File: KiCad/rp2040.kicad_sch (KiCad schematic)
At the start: 32 parts, among them SW1 SW_Push, U1 RP2040, U3 W25Q16JVSSIQ, Y1 12.000MHz

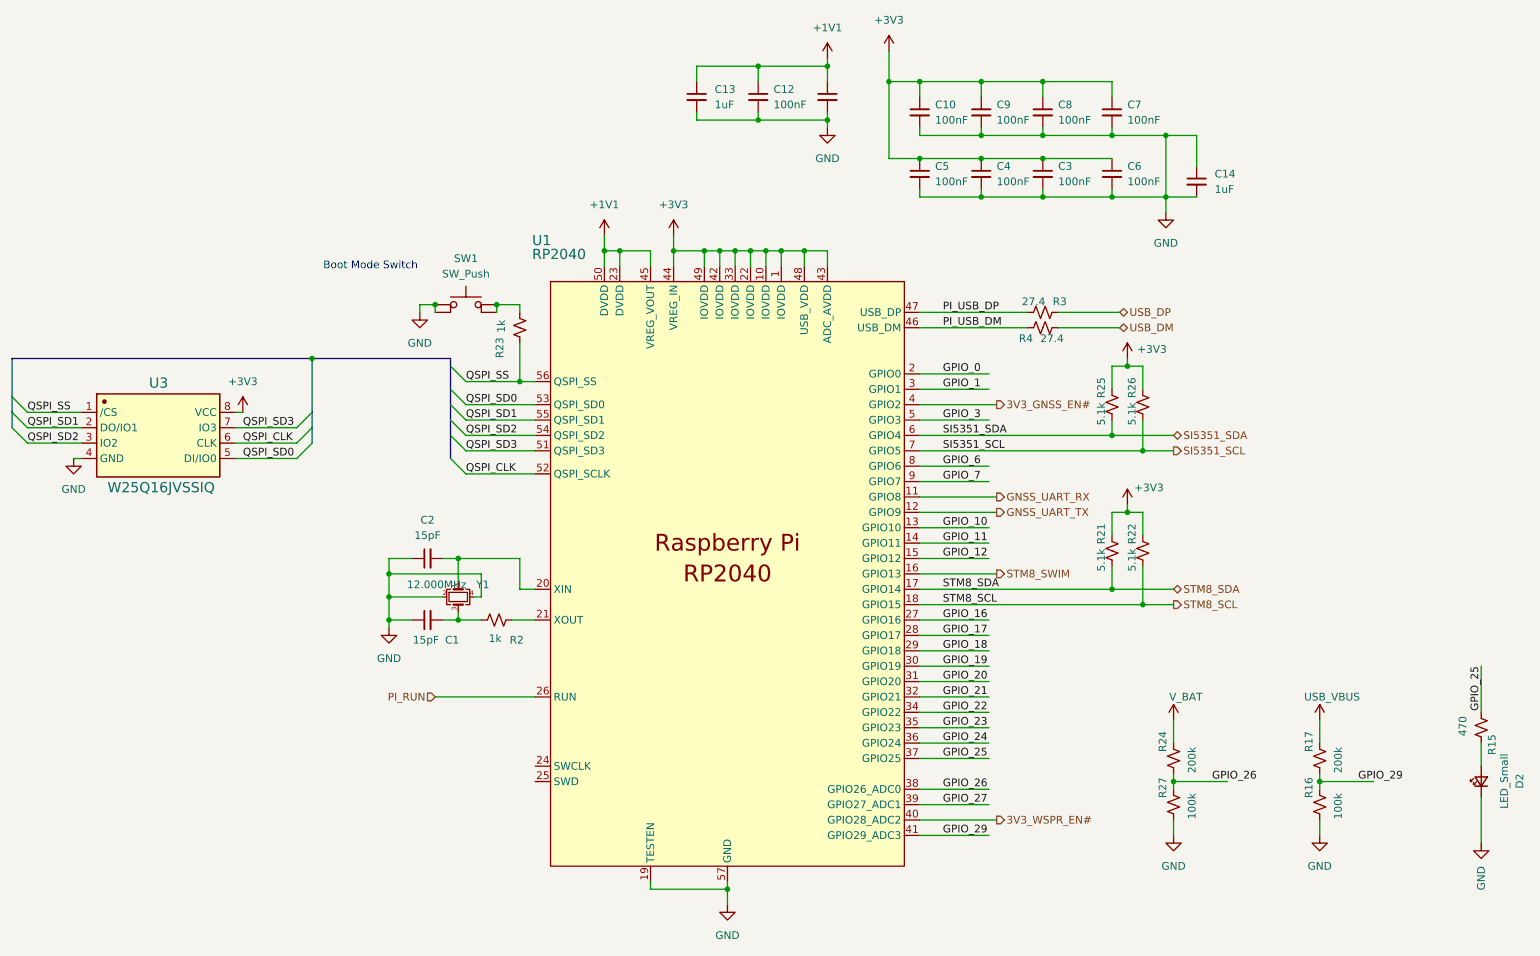
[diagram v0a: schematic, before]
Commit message: Start of docs and design incremental progress
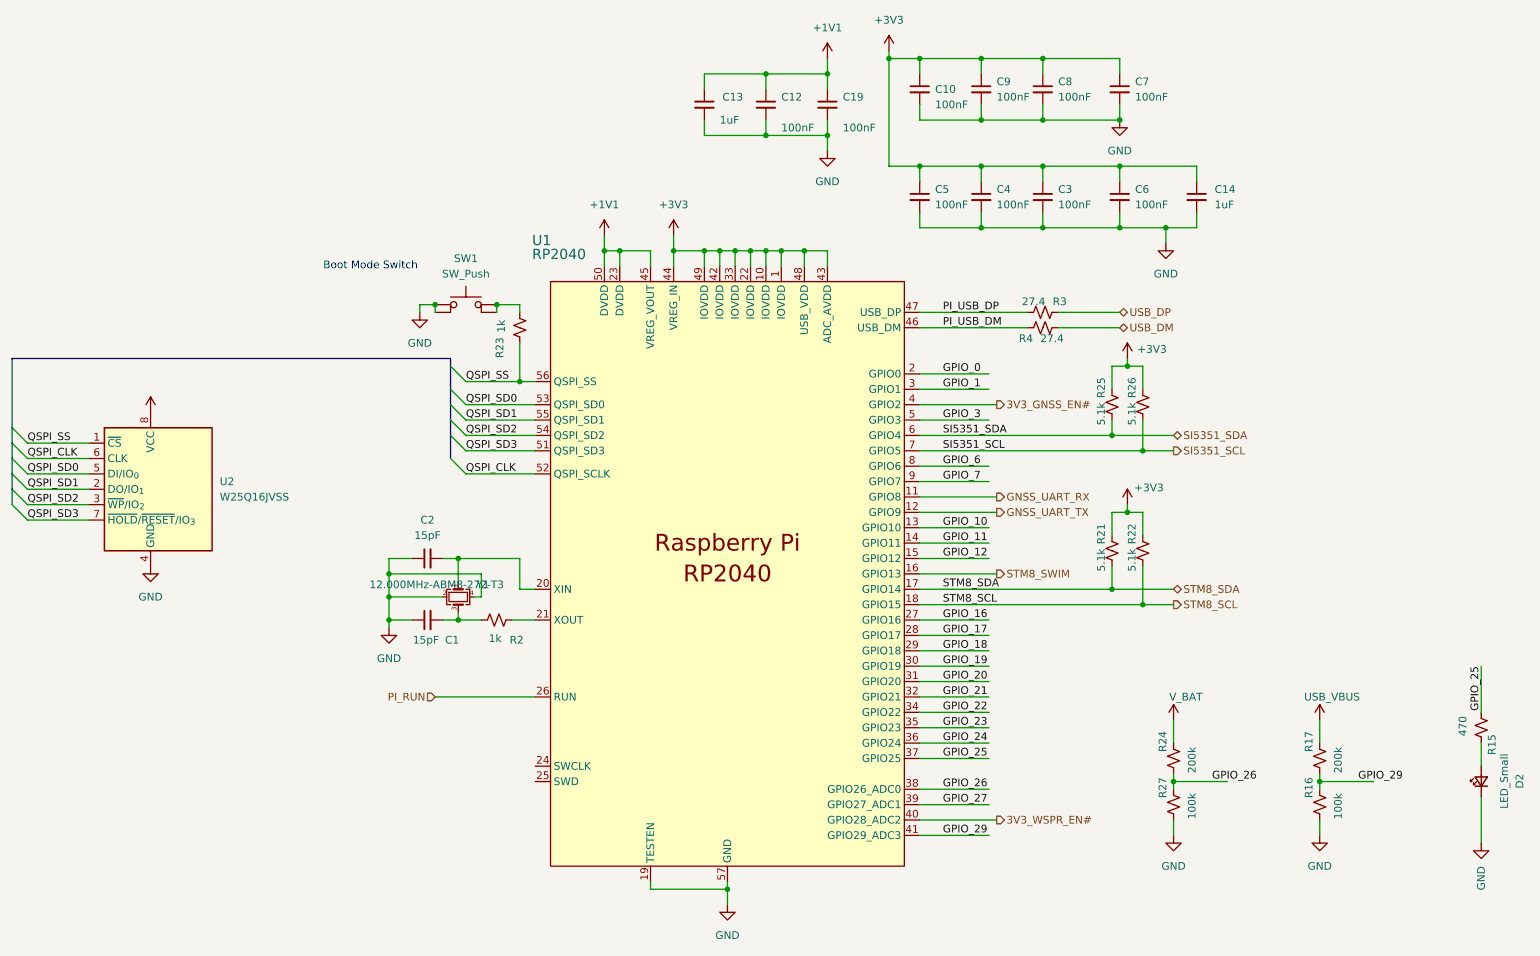
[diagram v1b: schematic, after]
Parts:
- removed C11: 100nF, Capacitor_SMD:C_0402_1005Metric, symbol Device:C_Small
- removed U3: W25Q16JVSSIQ, Package_SON:Winbond_USON-8-1EP_3x2mm_P0.5mm_EP0.2x1.6mm, symbol W25Q16JVSSIQ
- added C19: 100nF, Capacitor_SMD:C_0402_1005Metric, symbol Device:C_Small
- added U2: W25Q16JVSS, Package_SO:SOIC-8_5.3x5.3mm_P1.27mm, symbol Memory_Flash:W25Q16JVSS
- D2: footprint (none) -> LED_SMD:LED_0402_1005Metric
- U1: footprint JetBoard:LQFN-56_L7.0-W7.0-P0.4-EP -> Package_DFN_QFN:QFN-56-1EP_7x7mm_P0.4mm_EP3.2x3.2mm
- Y1: value 12.000MHz -> 12.000MHz-ABM8-272-T3; footprint (none) -> Crystal:Crystal_SMD_3225-4Pin_3.2x2.5mm
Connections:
- net +1V1: now also C19.1
- net +3V3: now also C14.1, U2.8 (VCC)
- net GND: now also SW1.2, C19.2, U2.4 (GND); no longer C14.1, SW1. (2)
- net QSPI_CLK: now also U2.6 (CLK)
- net QSPI_SD0: now also U2.5 (DI/IO_{0})
- net QSPI_SD1: now also U2.2 (DO/IO_{1})
- net QSPI_SD2: now also U2.3 (~{WP}/IO_{2})
- net QSPI_SD3: now also U2.7 (~{HOLD}/~{RESET}/IO_{3})
- net QSPI_SS: now also U2.1 (~{CS})
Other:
- moved on the sheet: C10, C12, C13, C14, C3, C4, C5, C6, C7, C8, C9

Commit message: Update schematic and board
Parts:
- U2: value W25Q16JVSS -> W25Q16JVUXIQ; footprint Package_SO:SOIC-8_5.3x5.3mm_P1.27mm -> Package_SON:Winbond_USON-8-1EP_3x2mm_P0.5mm_EP0.2x1.6mm
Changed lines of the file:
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@@
 			)
 		)
-		(property "Value" "W25Q16JVSS"
+		(property "Value" "W25Q16JVUXIQ"
 			(at 67.31 95.2499 0)
 			(effects
@@
 			)
 		)
-		(property "Footprint" "Package_SO:SOIC-8_5.3x5.3mm_P1.27mm"
+		(property "Footprint" "Package_SON:Winbond_USON-8-1EP_3x2mm_P0.5mm_EP0.2x1.6mm"
 			(at 55.88 93.98 0)
 			(effects
@@
 			)
 		)
-		(property "Description" "16Mbit / 2MiB Serial Flash Memory, Standard/Dual/Quad SPI, 2.7-3.6V, SOIC-8 (208 mil)"
+		(property "Description" "16Mbit / 2MiB Serial Flash Memory, Standard/Dual/Quad SPI, 2.7-3.6V"
 			(at 55.88 93.98 0)
 			(effects

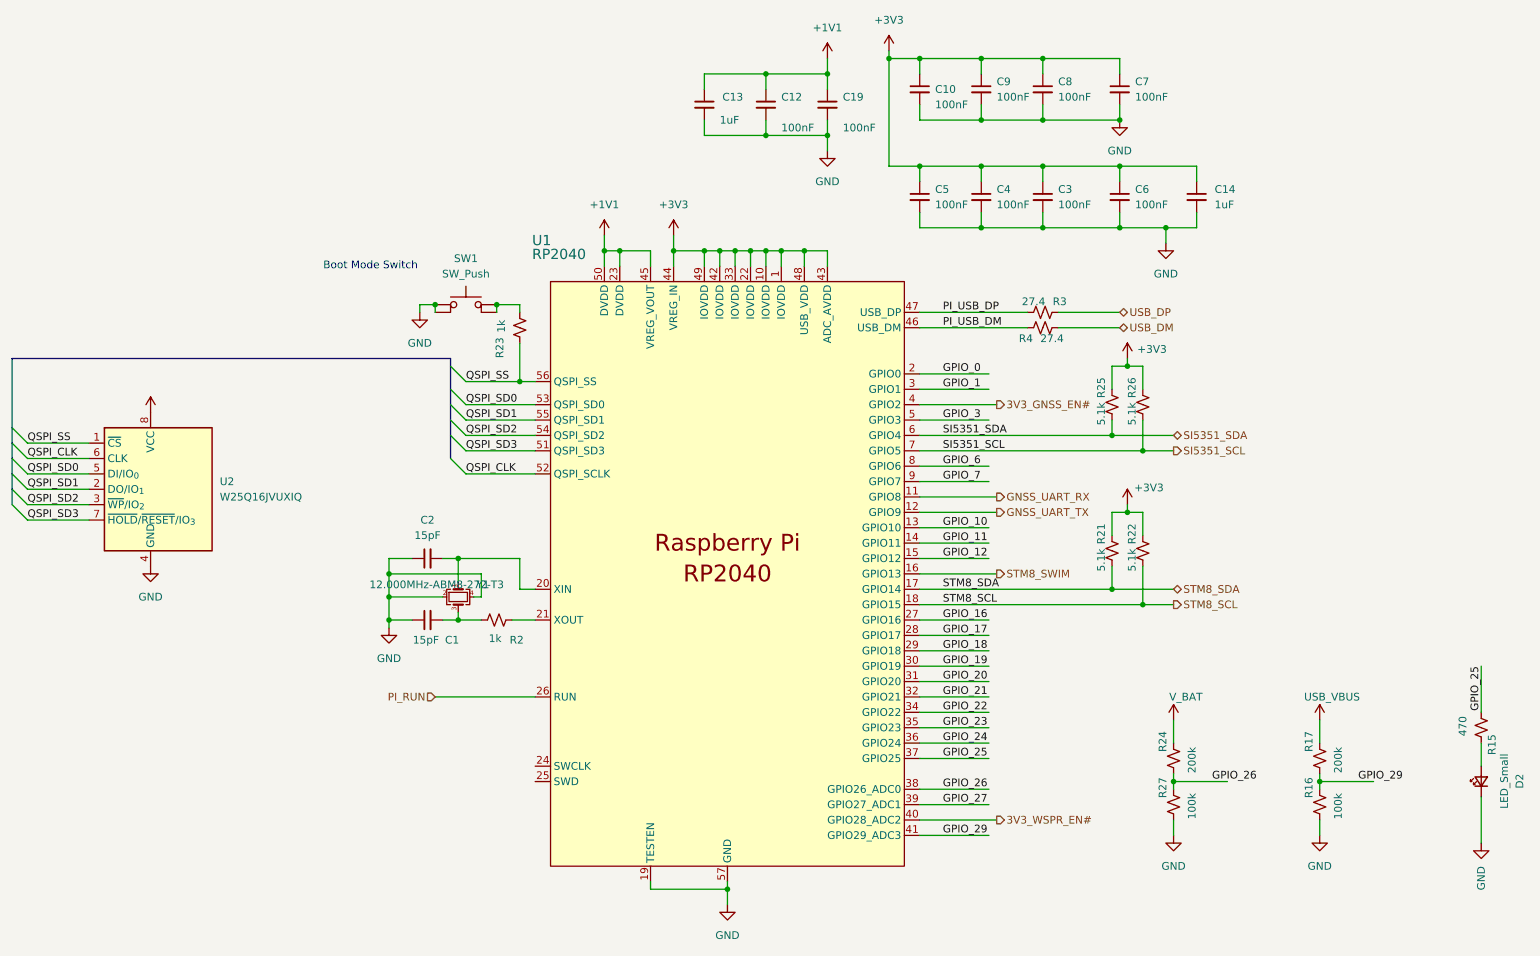
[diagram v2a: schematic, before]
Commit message: 3D model fixes and change to 3.0V buck
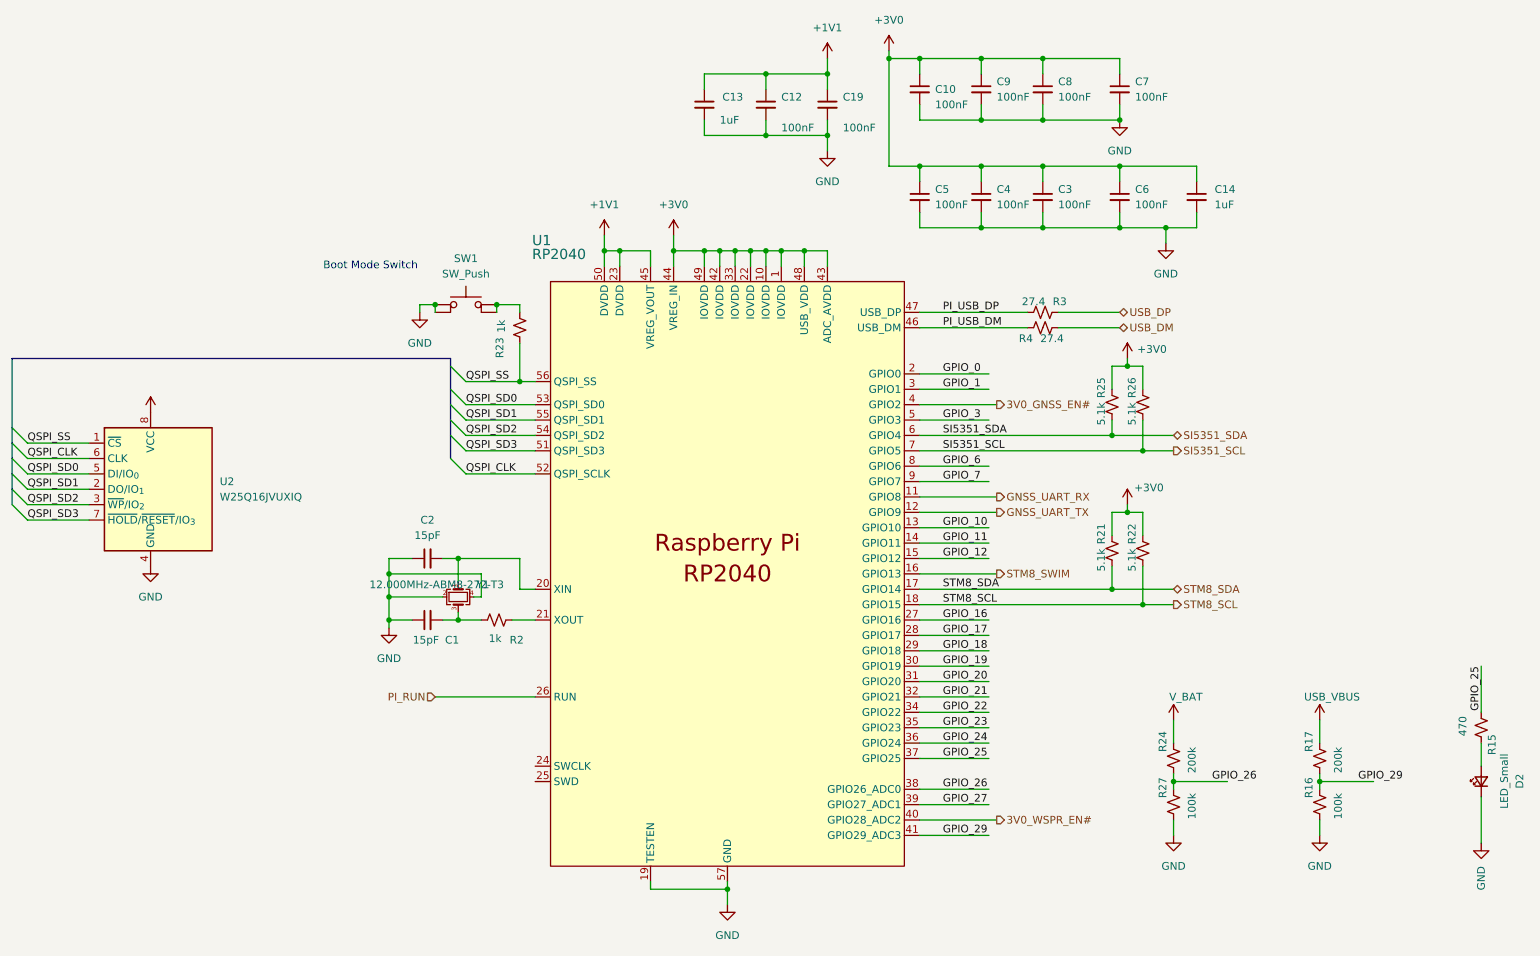
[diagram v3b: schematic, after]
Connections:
- net +3V3: no longer C10.1, C14.1, C3.1, C4.1, C5.1, C6.1, C7.1, C8.1, C9.1, R21.2, R22.2, R25.2, R26.2, U1.1 (IOVDD), U1.10 (IOVDD), U1.22 (IOVDD), U1.33 (IOVDD), U1.42 (IOVDD), U1.43 (ADC_AVDD), U1.44 (VREG_IN), U1.48 (USB_VDD), U1.49 (IOVDD)
- net 3V3_GNSS_EN# renamed 3V0_GNSS_EN#
- net 3V3_WSPR_EN# renamed 3V0_WSPR_EN#
- new net +3V0: C10.1, C14.1, C3.1, C4.1, C5.1, C6.1, C7.1, C8.1, C9.1, R21.2, R22.2, R25.2, R26.2, U1.1 (IOVDD), U1.10 (IOVDD), U1.22 (IOVDD), U1.33 (IOVDD), U1.42 (IOVDD), U1.43 (ADC_AVDD), U1.44 (VREG_IN), U1.48 (USB_VDD), U1.49 (IOVDD)
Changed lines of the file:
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@@
 		)
 	)
-	(hierarchical_label "3V3_GNSS_EN#"
+	(hierarchical_label "3V0_GNSS_EN#"
 		(shape output)
 		(at 195.58 80.01 0)
@@
 		)
 	)
-	(hierarchical_label "3V3_WSPR_EN#"
+	(hierarchical_label "3V0_WSPR_EN#"
 		(shape output)
 		(at 195.58 148.59 0)
@@
 			)
 		)
-		(property "Value" "+3V3"
+		(property "Value" "+3V0"
 			(at 220.726 93.726 0)
 			(effects
@@
 			)
 		)
-		(property "Value" "+3V3"
+		(property "Value" "+3V0"
 			(at 177.8 16.51 0)
 			(effects
@@
 			)
 		)
-		(property "Value" "+3V3"
+		(property "Value" "+3V0"
 			(at 142.24 46.99 0)
 			(effects
@@
 			)
 		)
-		(property "Value" "+3V3"
+		(property "Value" "+3V0"
 			(at 221.234 70.866 0)
 			(effects

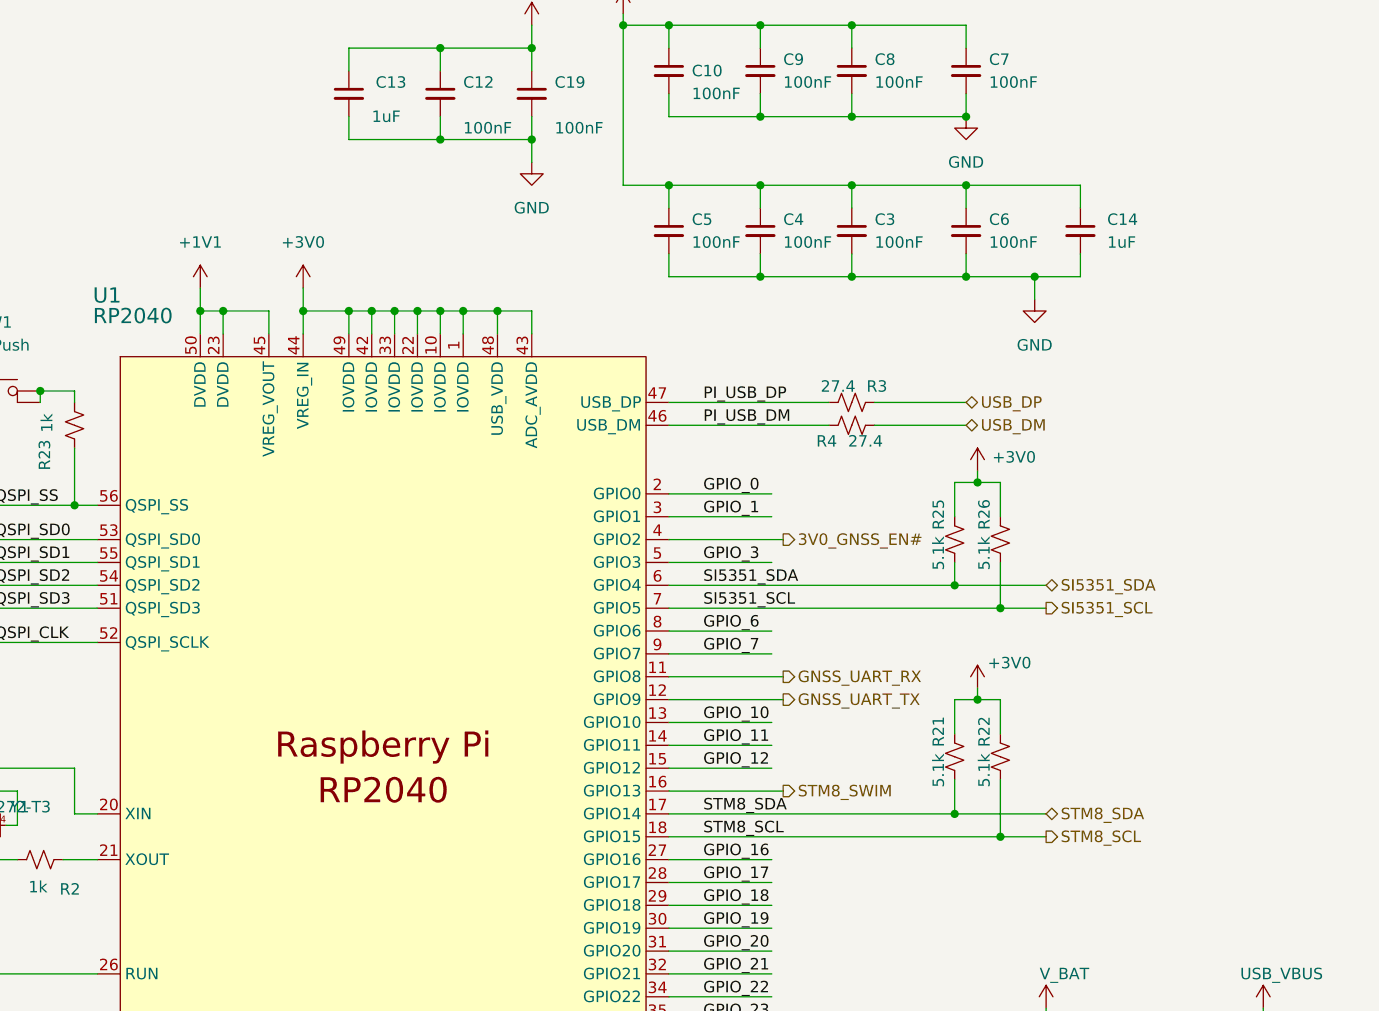
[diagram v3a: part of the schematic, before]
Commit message: Schematic changes
- Changed to STM8L050
- Changed to SPI interface for STM8 bootloader
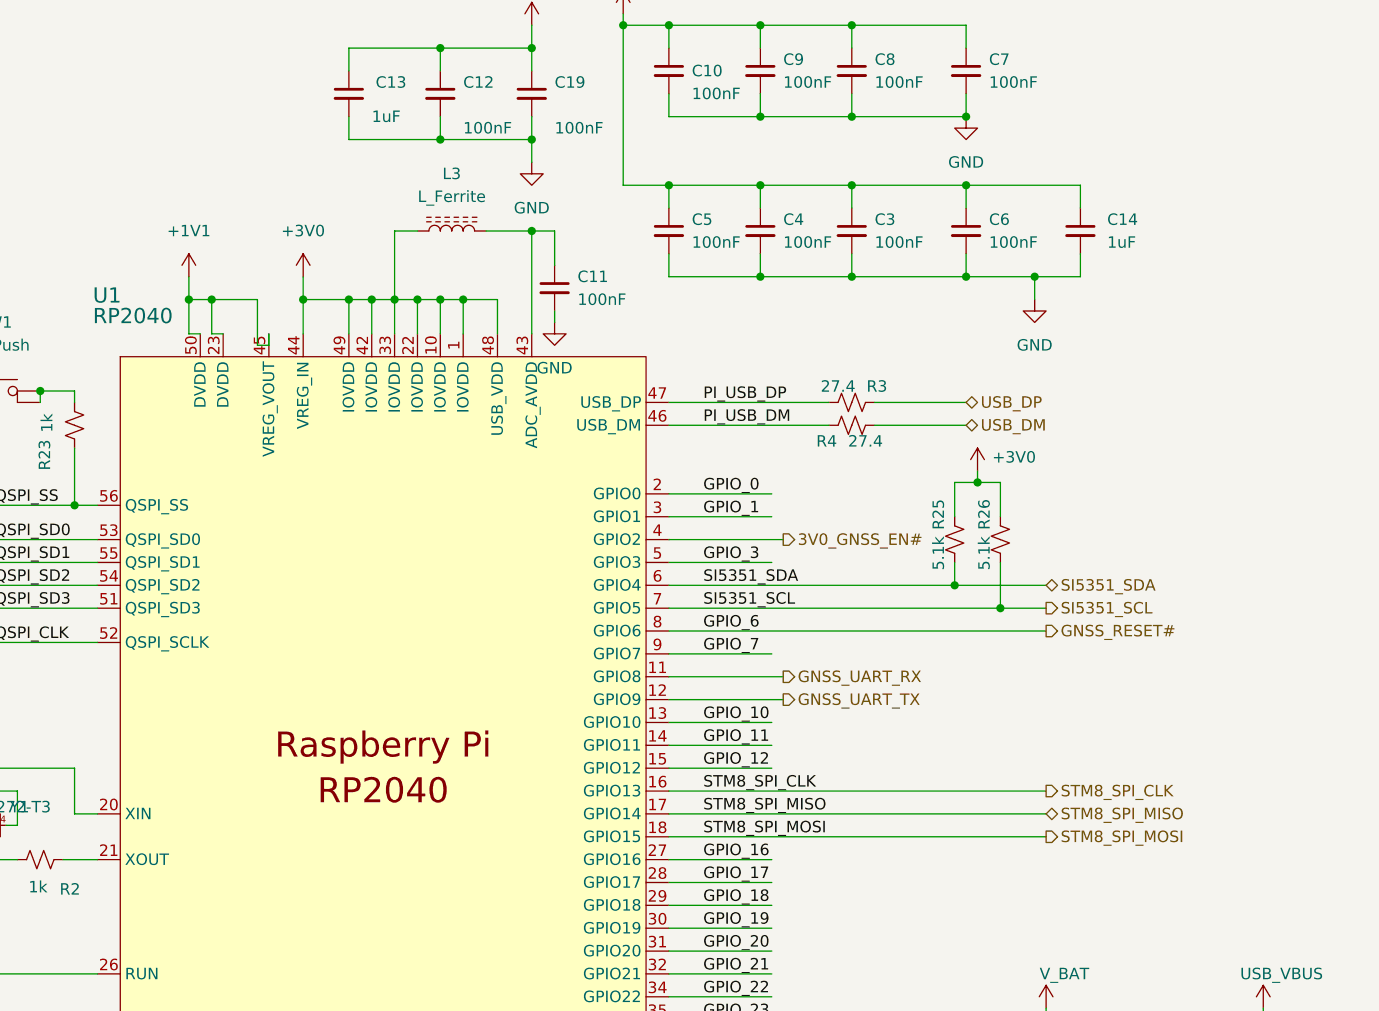
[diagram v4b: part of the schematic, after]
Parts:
- removed R21, R22: 5.1k, Resistor_SMD:R_0402_1005Metric, symbol Device:R_Small_US
- added C11: 100nF, Capacitor_SMD:C_0402_1005Metric, symbol Device:C_Small
- added L3: L_Ferrite, symbol Device:L_Ferrite
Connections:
- net +3V0: now also L3.1; no longer U1.43 (ADC_AVDD)
- net GND: now also C11.2
- net GPIO_6 renamed GNSS_RESET#
- net STM8_SCL renamed STM8_SPI_MOSI
- net STM8_SDA renamed STM8_SPI_MISO
- net STM8_SWIM renamed STM8_SPI_CLK
- new net: C11.1, L3.2, U1.43 (ADC_AVDD)
